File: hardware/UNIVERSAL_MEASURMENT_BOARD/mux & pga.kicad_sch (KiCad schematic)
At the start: 11 parts, among them U11 CD4097BM, U4 PGA280AIPW

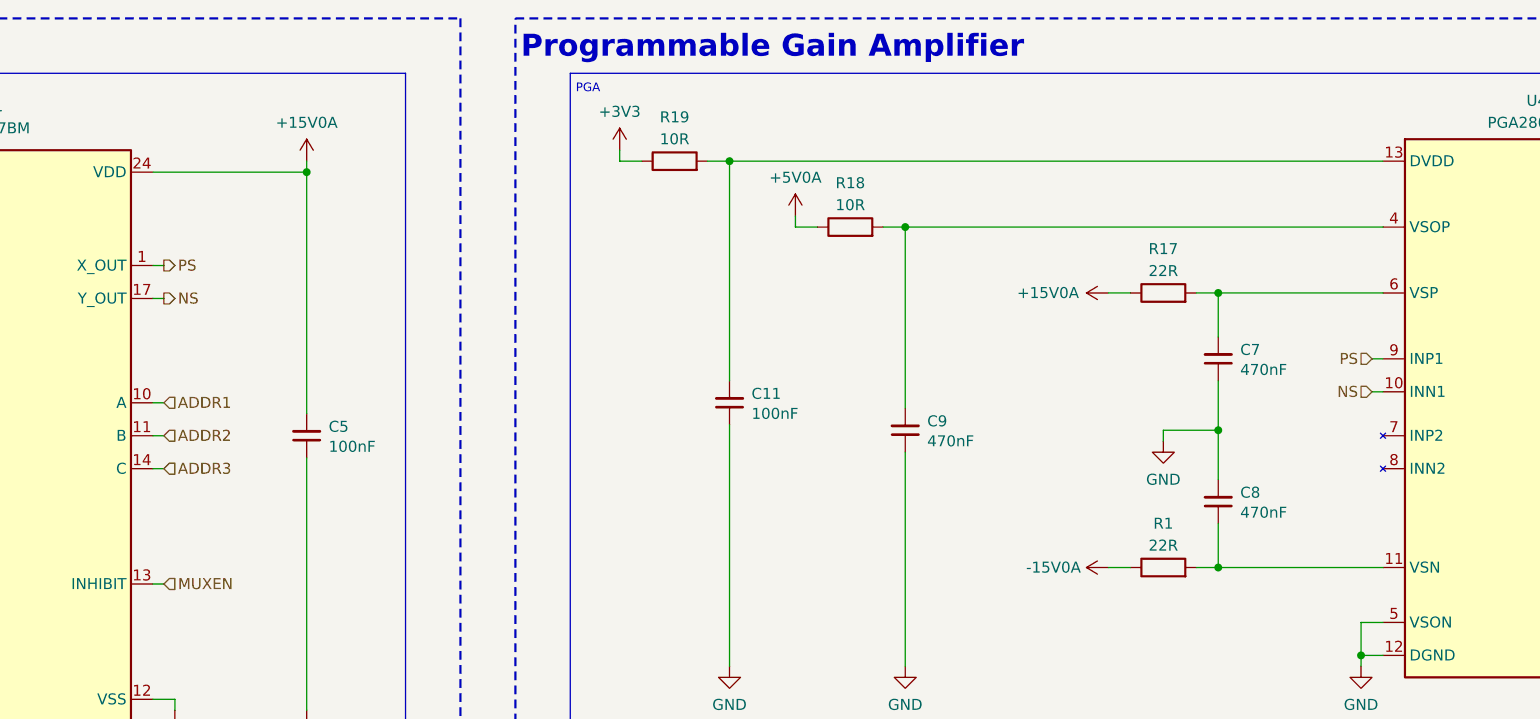
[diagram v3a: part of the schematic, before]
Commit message: added footprints
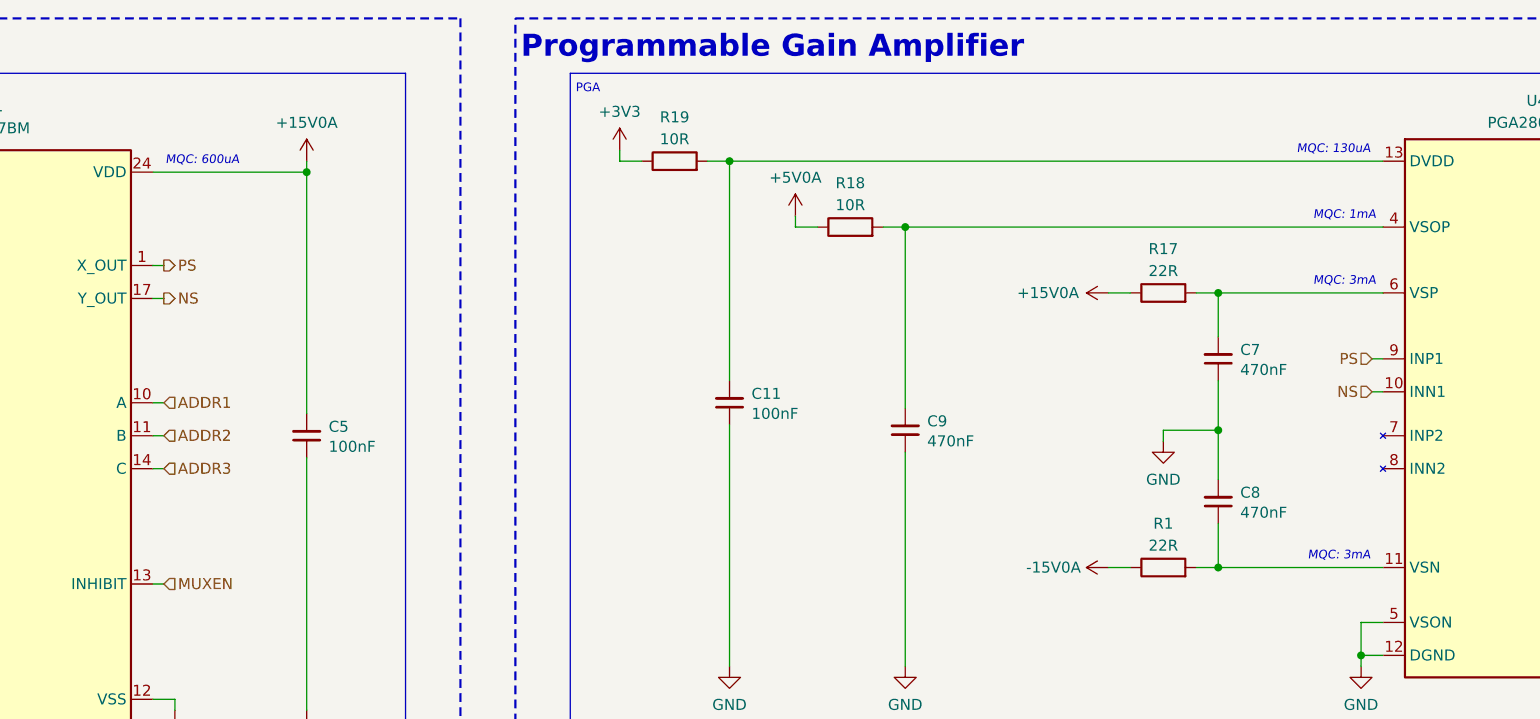
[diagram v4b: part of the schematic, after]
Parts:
- C11, C5, C7, C8, C9: footprint Capacitor_SMD:C_0805_2012Metric -> Capacitor_SMD:C_0603_1608Metric
- R1, R17, R18, R19: footprint (none) -> Resistor_SMD:R_0603_1608Metric
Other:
- note added: "MQC: 130uA"
- note added: "MQC: 1mA"
- note added: "MQC: 3mA"
- note added: "MQC: 600uA"
- company: PUT Motorsport Formula Student team -> PUT Motorsport Formula Student Team
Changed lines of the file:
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@@
 		(title "Universal Measurment Board")
 		(date "2026-02-02")
-		(rev "1.7.14")
-		(company "PUT Motorsport Formula Student team")
+		(rev "1.7.15")
+		(company "PUT Motorsport Formula Student Team")
 		(comment 1 "Designed by Marcin Trzmiel under")
 	)
@@
 		(fill
 			(type none)
+		)
+	)
+	(text "MQC: 130uA"
+		(exclude_from_sim no)
+		(at 267.335 99.06 0)
+		(effects
+			(font
+				(size 1 1)
+				(italic yes)
+				(color 105 110 255 0.3490196078)
+			)
 		)
 	)
@@
 		)
 	)
+	(text "MQC: 1mA"
+		(exclude_from_sim no)
+		(at 268.605 106.68 0)
+		(effects
+			(font
+				(size 1 1)
+				(italic yes)
+				(color 105 110 255 0.3490196078)
+			)
+		)
+	)
 	(text "PGA"
 		(exclude_from_sim no)
@@
 			)
 			(justify left top)
+		)
+	)
+	(text "MQC: 600uA"
+		(exclude_from_sim no)
+		(at 136.525 100.33 0)
+		(effects
+			(font
+				(size 1 1)
+				(italic yes)
+				(color 105 110 255 0.3490196078)
+			)
+		)
+	)
+	(text "MQC: 3mA"
+		(exclude_from_sim no)
+		(at 268.605 114.3 0)
+		(effects
+			(font
+				(size 1 1)
+				(italic yes)
+				(color 105 110 255 0.3490196078)
+			)
+		)
+	)
+	(text "MQC: 3mA"
+		(exclude_from_sim no)
+		(at 267.97 146.05 0)
+		(effects
+			(font
+				(size 1 1)
+				(italic yes)
+				(color 105 110 255 0.3490196078)
+			)
 		)
 	)
@@
 			)
 		)
-		(property "Footprint" ""
+		(property "Footprint" "Resistor_SMD:R_0603_1608Metric"
 			(at 247.65 117.348 90)
 			(effects
@@
 			)
 		)
-		(property "Footprint" "Capacitor_SMD:C_0805_2012Metric"
+		(property "Footprint" "Capacitor_SMD:C_0603_1608Metric"
 			(at 254 139.7 0)
 			(effects
@@
 			)
 		)
-		(property "Footprint" "Capacitor_SMD:C_0805_2012Metric"
+		(property "Footprint" "Capacitor_SMD:C_0603_1608Metric"
 			(at 217.805 131.445 0)
 			(effects
@@
 			)
 		)
-		(property "Footprint" ""
+		(property "Footprint" "Resistor_SMD:R_0603_1608Metric"
 			(at 211.455 109.728 90)
 			(effects
@@
 			)
 		)
-		(property "Footprint" "Capacitor_SMD:C_0805_2012Metric"
+		(property "Footprint" "Capacitor_SMD:C_0603_1608Metric"
 			(at 254 123.19 0)
 			(effects
@@
 			)
 		)
-		(property "Footprint" "Capacitor_SMD:C_0805_2012Metric"
+		(property "Footprint" "Capacitor_SMD:C_0603_1608Metric"
 			(at 148.59 132.08 0)
 			(effects
@@
 			)
 		)
-		(property "Footprint" ""
+		(property "Footprint" "Resistor_SMD:R_0603_1608Metric"
 			(at 191.135 102.108 90)
 			(effects
@@
 			)
 		)
-		(property "Footprint" "Capacitor_SMD:C_0805_2012Metric"
+		(property "Footprint" "Capacitor_SMD:C_0603_1608Metric"
 			(at 197.485 128.27 0)
 			(effects
@@
 			)
 		)
-		(property "Footprint" ""
+		(property "Footprint" "Resistor_SMD:R_0603_1608Metric"
 			(at 247.65 149.098 90)
 			(effects

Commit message: first outcom of pcb design
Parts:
- C10: renamed from C8; footprint Capacitor_SMD:C_0603_1608Metric -> REST:C_0603_1608Metric
- C11: renamed from C5; footprint Capacitor_SMD:C_0603_1608Metric -> REST:C_0603_1608Metric
- C7: renamed from C11; footprint Capacitor_SMD:C_0603_1608Metric -> REST:C_0603_1608Metric
- C8: renamed from C9; footprint Capacitor_SMD:C_0603_1608Metric -> REST:C_0603_1608Metric
- C9: renamed from C7; footprint Capacitor_SMD:C_0603_1608Metric -> REST:C_0603_1608Metric
- R1: renamed from R19; footprint Resistor_SMD:R_0603_1608Metric -> REST:R_0603_1608Metric
- R2: renamed from R18; footprint Resistor_SMD:R_0603_1608Metric -> REST:R_0603_1608Metric
- R3: renamed from R17; footprint Resistor_SMD:R_0603_1608Metric -> REST:R_0603_1608Metric
- R4: renamed from R1; footprint Resistor_SMD:R_0603_1608Metric -> REST:R_0603_1608Metric
- renumbered U4 to U3, U11 to U4
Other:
- moved on the sheet: C10, C11, C7, C8, C9, R1, R2, R3, R4, U3, U4

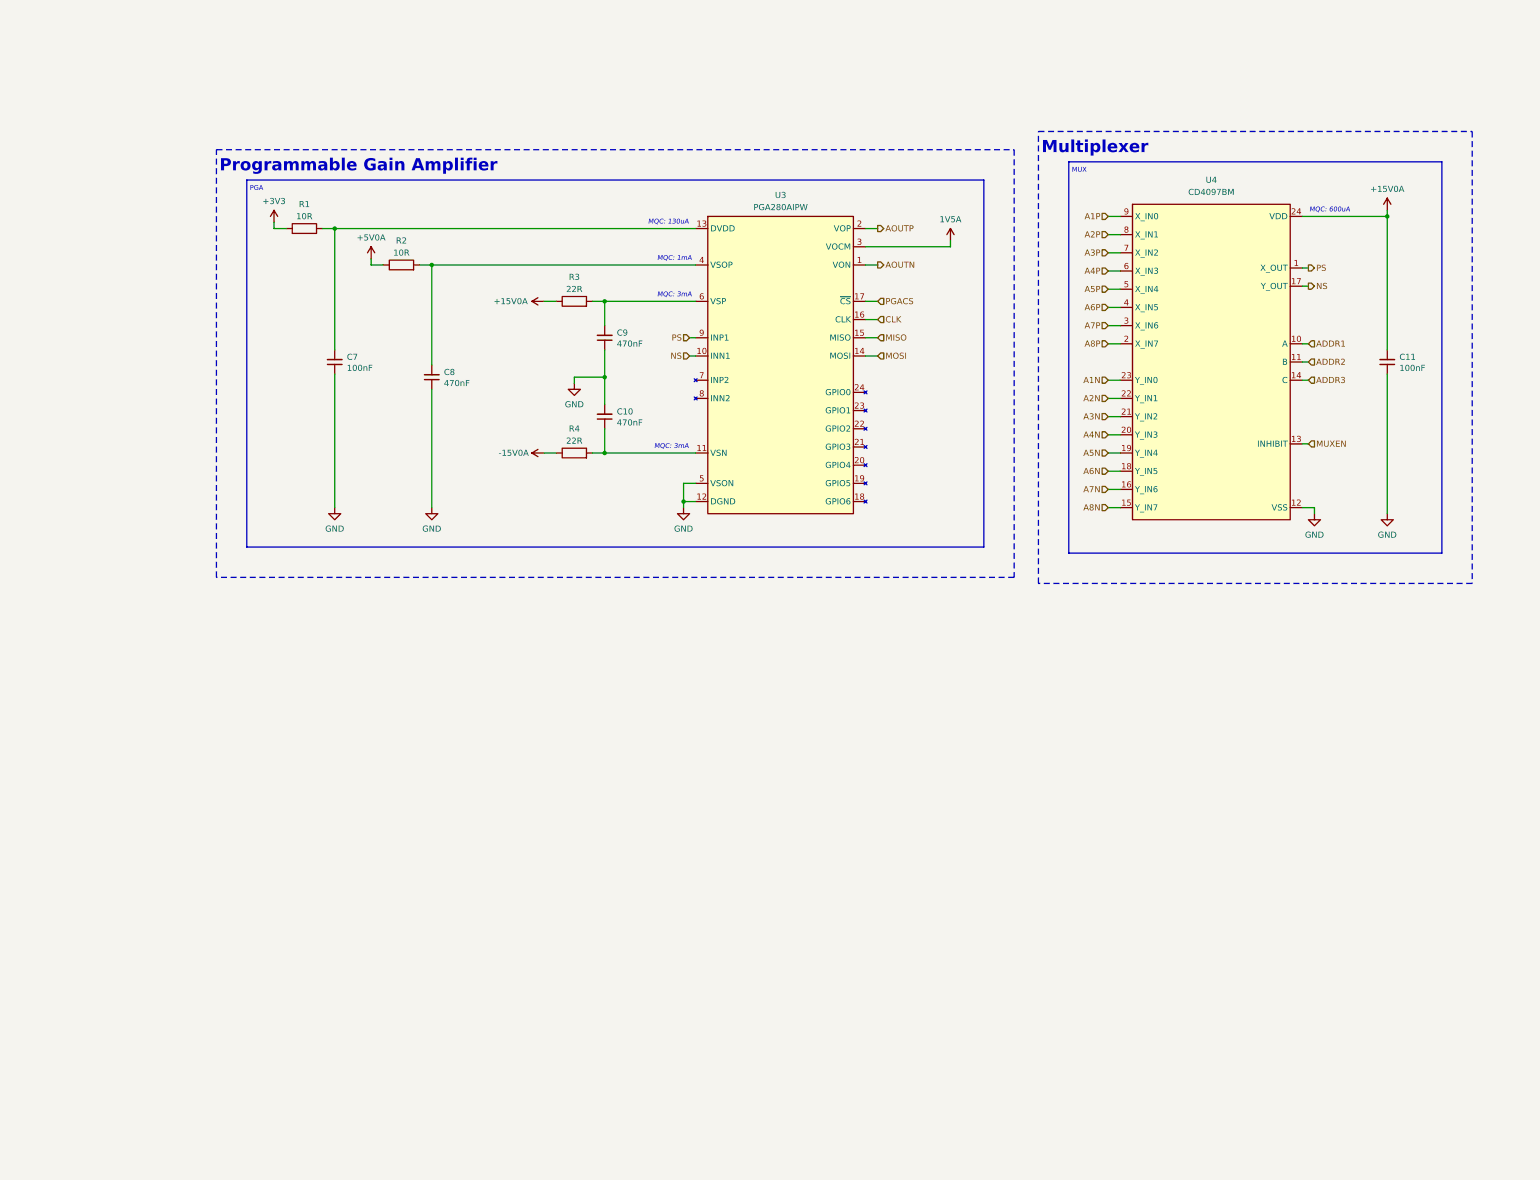
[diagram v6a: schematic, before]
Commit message: Solved ERC problems
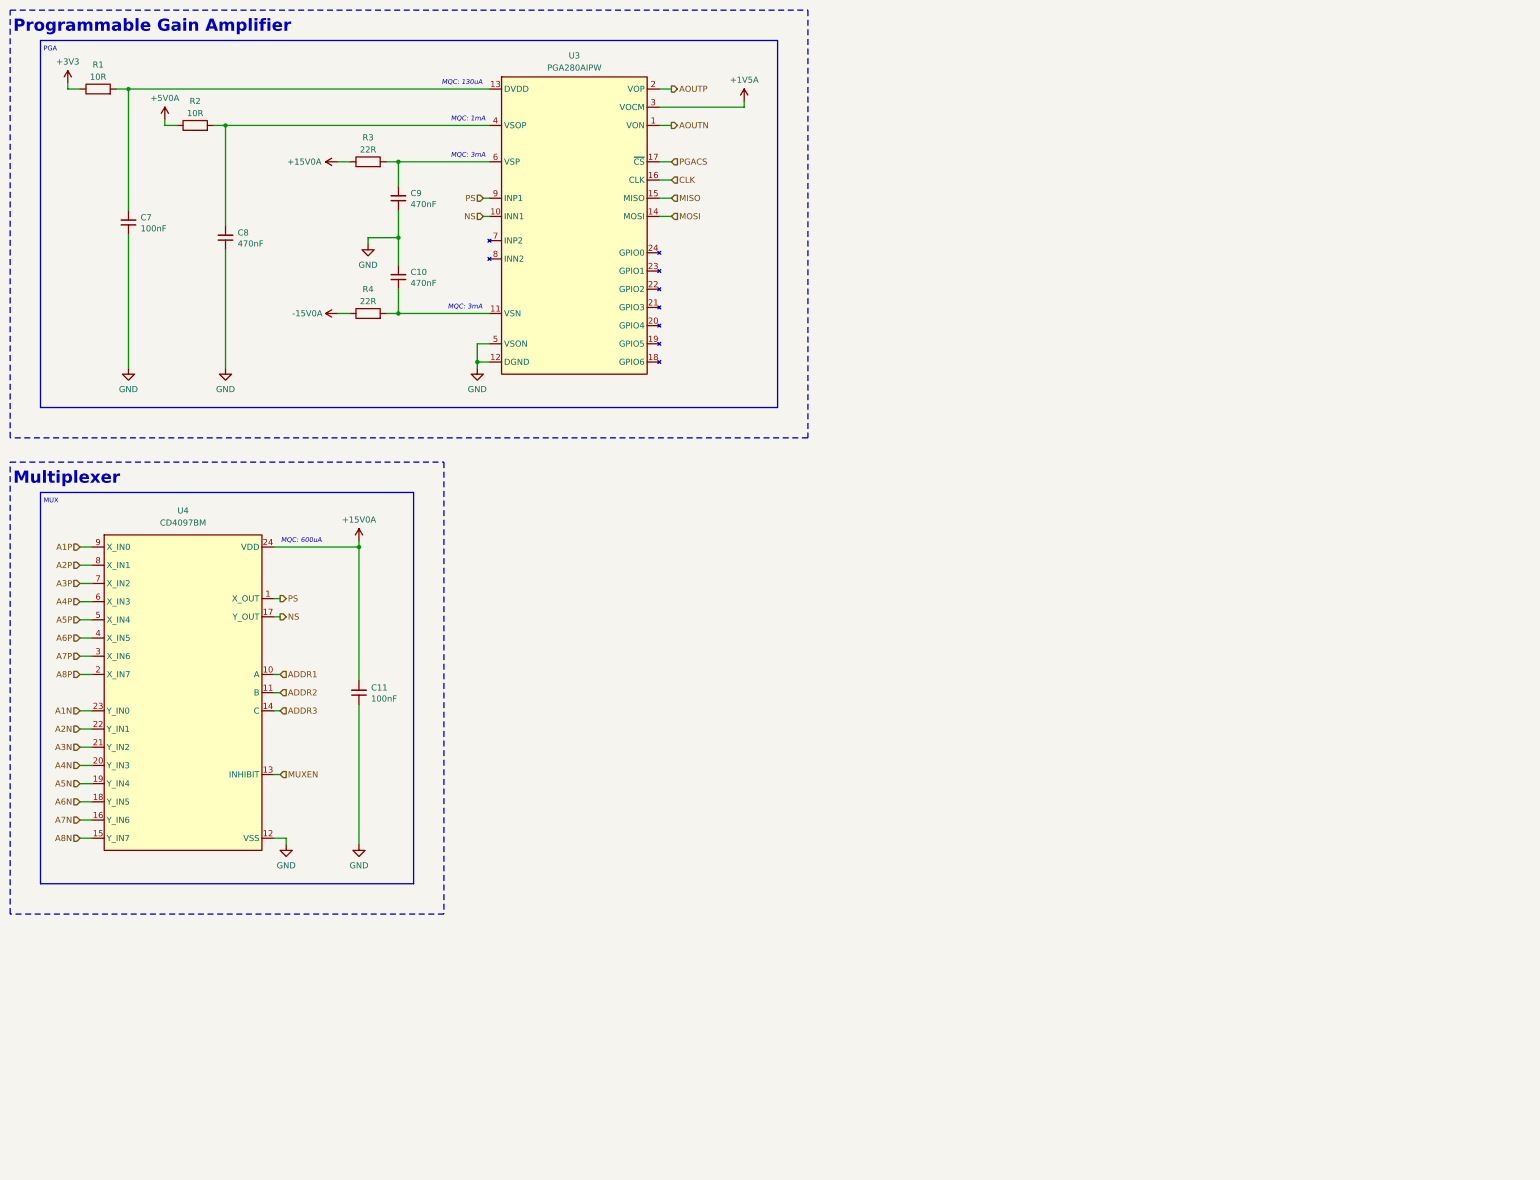
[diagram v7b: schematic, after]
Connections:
- net 1V5A renamed +1V5A
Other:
- moved on the sheet: C10, C11, C7, C8, C9, R1, R2, R3, R4, U3, U4
